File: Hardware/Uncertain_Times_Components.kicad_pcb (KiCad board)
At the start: 4 copper layers, 80.8 x 100 mm, 197 parts, among them J1 Conn_01x12_Male, J2 Conn_01x16_Male, J3 Conn_01x14_Male, J4 Conn_01x12_Male, J5 SWD_Header, J6 Eurorack_10_pin_power, J7 Audio_Breakout, J8 Gate_Breakout, Q1 MMBT3904, U1 LM1117-3.3, U10 TL074, U11 TL074, U12 TL074, U13 TL074, U14 TL074, U15 TL074, U2 STM32G473V, U3 LM1117-5.0, U4 PS508, U5 MCP6002, U6 AS3364, U7 AS3364, U8 AD5676, U9 MCP48CMB21, Y1 8MHz 20pF

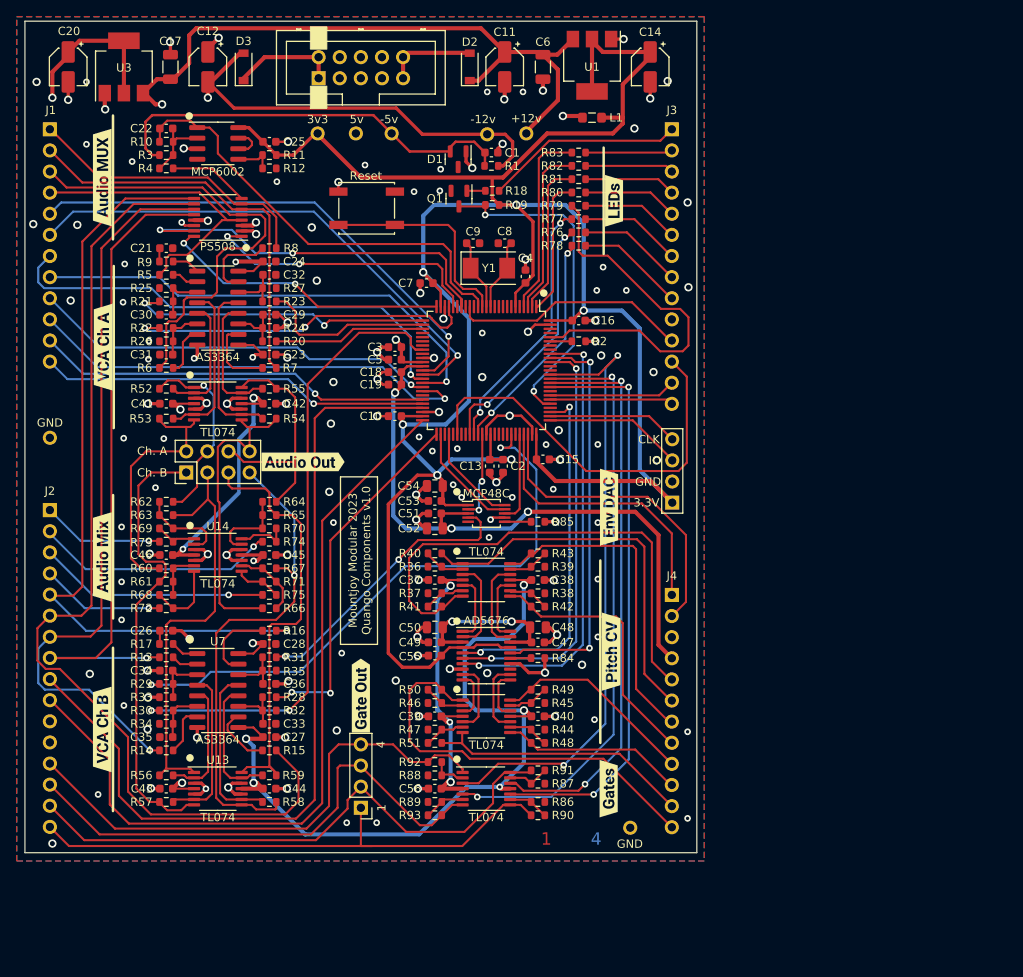
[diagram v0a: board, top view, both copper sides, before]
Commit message: Started routing components
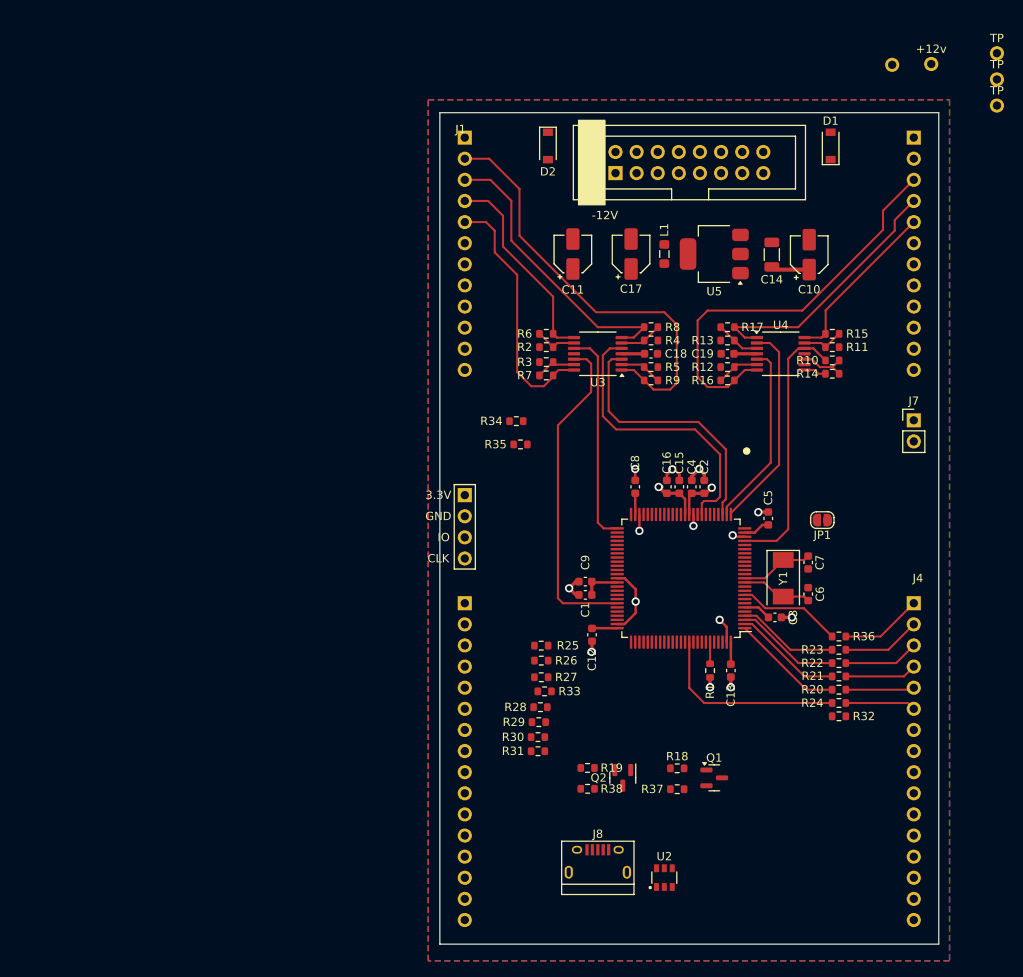
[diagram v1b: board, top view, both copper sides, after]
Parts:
- removed the C1 at (106.2, 54.8)
- removed the C17 at (67.6, 44.5)
- removed C20: 22uF, Capacitor_SMD:CP_Elec_4x5.8
- removed C21, C26: 10nF, Capacitor_SMD:C_0603_1608Metric
- removed C22: 1.5nF, Capacitor_SMD:C_0603_1608Metric
- removed C23, C24, C27, C28, C37, C38, C39, C40, C41, C42, C43, C44, C45, C46, C47, C49, C51, C53, C55, C56: 100nF, Capacitor_SMD:C_0603_1608Metric
- removed C25: 1uF, Capacitor_SMD:C_0603_1608Metric
- removed C29, C30, C31, C32, C33, C34, C35, C36: 2.2nF, Capacitor_SMD:C_0603_1608Metric
- removed C48, C50, C52, C54: 10uF, Capacitor_SMD:C_0805_2012Metric
- removed the D1 at (102.2, 55.6)
- removed FID1: Fiducial, Custom_Footprints:4_Layer_Markers
- removed the R1 at (106.2, 56.4)
- removed the R20 at (79.5, 77.5)
- removed the R21 at (67.1, 72.7)
- removed the R22 at (67.1, 75.9)
- removed the R23 at (79.5, 72.7)
- removed the R24 at (79.5, 75.9)
- removed the R25 at (67.1, 71.1)
- removed the R26 at (67.1, 77.5)
- removed the R27 at (79.5, 71.1)
- removed the R38 at (111.8, 107.8)
- removed R39, R44, R45, R46, R47, R60, R61, R62, R63, R64, R65, R66, R67, R68, R69, R70, R71, R86, R87, R88, R89: 10k, Resistor_SMD:R_0603_1608Metric
- removed R40, R41, R42, R43, R48, R49, R50, R51: 2k, Resistor_SMD:R_0603_1608Metric
- removed R52, R53, R54, R55, R56, R57, R58, R59: 30k, Resistor_SMD:R_0603_1608Metric
- removed R72, R73, R74, R75: 1k, Resistor_SMD:R_0603_1608Metric
- removed R84, R85: 560, Resistor_SMD:R_0603_1608Metric
- removed R90, R91, R92, R93: 15k, Resistor_SMD:R_0603_1608Metric
- removed RESET1: SW_Push, Custom_Footprints:SW_SPST_EVQQ2
- removed TP6, TP7: TestPoint, Custom_Footprints:1mm_Test_Point
- removed the U1 at (118.3, 44.3)
- removed U10, U11, U12, U13, U14, U15: TL074, Package_SO:TSSOP-14_4.4x5mm_P0.65mm
- removed U6, U7: AS3364, Package_SO:SOIC-16_3.9x9.9mm_P1.27mm
- removed U8: AD5676, Package_SO:TSSOP-20_4.4x6.5mm_P0.65mm
- removed U9: MCP48CMB21, Package_SO:MSOP-10_3x3mm_P0.5mm
- removed kibuzzard-646A0602: G***, kibuzzard-646A0602
- removed kibuzzard-646A061F: G***, kibuzzard-646A061F
- removed kibuzzard-646A06F2: G***, kibuzzard-646A06F2
- removed kibuzzard-646A076E: G***, kibuzzard-646A076E
- removed kibuzzard-646B918A: G***, kibuzzard-646B918A
- removed kibuzzard-646B919C: G***, kibuzzard-646B919C
- removed kibuzzard-646B91AE: G***, kibuzzard-646B91AE
- removed kibuzzard-646B91BF: G***, kibuzzard-646B91BF
- removed kibuzzard-646B935C: G***, kibuzzard-646B935C
- removed kibuzzard-646B9368: G***, kibuzzard-646B9368
- added C18: 100nF, Capacitor_SMD:C_0603_1608Metric, F.Cu at (125.4, 79.0)
- added C19: 100nF, Capacitor_SMD:C_0603_1608Metric, F.Cu at (134.6, 79.0)
- added JP1: Jumper, Jumper:SolderJumper-2_P1.3mm_Open_RoundedPad1.0x1.5mm, F.Cu at (146.0, 99.0)
- added Q1: MMBT3904, Package_TO_SOT_SMD:SOT-23, F.Cu at (133.0, 130.0)
- added R18: 4k7, Resistor_SMD:R_0603_1608Metric, F.Cu at (128.6, 128.9)
- added R2: 10k, Resistor_SMD:R_0603_1608Metric, F.Cu at (112.8, 78.2)
- added U2: STF202-22T1G, Custom_Footprints:STF202-22T1G, F.Cu at (127.0, 142.0)
- C10: renamed from C11; value 47uF -> 22uF
- J2: value Conn_01x16_Male -> Conn_01x12_Male; footprint Connector_PinHeader_2.54mm:PinHeader_1x16_P2.54mm_Vertical -> Connector_PinHeader_2.54mm:PinHeader_1x12_P2.54mm_Vertical
- J3: value Conn_01x14_Male -> Conn_01x16_Male; footprint Connector_PinHeader_2.54mm:PinHeader_1x14_P2.54mm_Vertical -> Connector_PinHeader_2.54mm:PinHeader_1x16_P2.54mm_Vertical
- J4: value Conn_01x12_Male -> Conn_01x16_Male; footprint Connector_PinHeader_2.54mm:PinHeader_1x12_P2.54mm_Vertical -> Connector_PinHeader_2.54mm:PinHeader_1x16_P2.54mm_Vertical
- J6: value Eurorack_10_pin_power -> Eurorack_16_pin_power; footprint Custom_Footprints:Eurorack_10_pin_header -> Custom_Footprints:Eurorack_16_pin_header
- J7: value Audio_Breakout -> UART_Test_Pins; footprint Connector_PinHeader_2.54mm:PinHeader_2x04_P2.54mm_Vertical -> Connector_PinHeader_2.54mm:PinHeader_1x02_P2.54mm_Vertical
- J8: value Gate_Breakout -> USB_B_Micro; footprint Connector_PinHeader_2.54mm:PinHeader_1x04_P2.54mm_Vertical -> Custom_Footprints:USB_Micro-B_Amphenol
- R10: value 6k8 -> 10k
- R13, R15, R16, R5, R6, R7, R8: value 30k -> 10k
- R14: value 30k -> 20k
- R17, R9: value 100R -> 10k
- R28, R29, R30, R31: value 6k8 -> 560
- R3: value 20k -> 10k
- R32, R33, R34, R35, R36: value 10k -> 560
- R37: value 10k -> 4k7
- R4: value 47k -> 10k
- U3: value LM1117-5.0 -> TL074; footprint Package_TO_SOT_SMD:SOT-223-3_TabPin2 -> Package_SO:TSSOP-14_4.4x5mm_P0.65mm
- U4: value PS508 -> TL074; footprint Package_SO:TSSOP-16_4.4x5mm_P0.65mm -> Package_SO:TSSOP-14_4.4x5mm_P0.65mm
- U5: value MCP6002 -> LT1117-3.3; footprint Package_SO:SOIC-8_3.9x4.9mm_P1.27mm -> Package_TO_SOT_SMD:SOT-223-3_TabPin2
- moved J2 113.1 mm to (157.0, 53.0)
- moved R14 92.0 mm to (147.2, 81.4), turned to 0 degrees
- moved J7 87.7 mm to (157.0, 87.0), turned to 0 degrees
- moved R10 84.3 mm to (147.2, 79.8), turned to 180 degrees
- moved R15 84.2 mm to (147.2, 76.6)
- moved TP5 81.8 mm to (167.0, 49.1)
- moved TP3 77.7 mm to (167.0, 42.9)
- moved R13 77.5 mm to (134.6, 77.4), turned to 0 degrees
- moved R17 77.5 mm to (134.6, 75.8), turned to 180 degrees
- moved TP4 73.1 mm to (167.0, 46.0)
- moved Q2 72.4 mm to (122.0, 130.0)
- moved R11 71.5 mm to (147.2, 78.2), turned to 180 degrees
- moved R38 71.2 mm to (117.8, 131.3)
- moved R19 70.4 mm to (117.8, 128.8)
- moved U4 69.7 mm to (141.0, 79.0), turned to 0 degrees
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- renumbered C2 to C1, C12 to C11, C15 to C12, C16 to C13, C6 to C14, C18 to C15, C19 to C16, C14 to C17, C3 to C2, C4 to C3, C5 to C4, C7 to C5, C8 to C6, C9 to C7, C10 to C8, C13 to C9, D2 to D1, D3 to D2, Q1 to Q2, R2 to R1, R18 to R19, R76 to R20, R77 to R21, R78 to R22, R79 to R23, R80 to R24, R81 to R25, R82 to R26, R83 to R27, R19 to R38, U2 to U1
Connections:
- J1 pad 1: /AudioA4_In -> GND
- J1 pad 10: /Env2_Decay -> GND
- J1 pad 11: /Env2_Sustain -> /Sine1_Level
- J1 pad 12: /Env2_Release -> /Sine2_Level
- J1 pad 2: /AudioA3_In -> /FM3_Out
- J1 pad 3: /AudioA2_In -> /FM2_Out
- J1 pad 4: /AudioA1_In -> /Ramp_Out
- J1 pad 5: /Env1_Attack -> /Swell_Out
- J1 pad 6: /Env1_Decay -> /Sine2_Rate_Btn
- J1 pad 7: /Env1_Sustain -> /Sine3_Rate_Btn
- J1 pad 8: /Env1_Release -> /Sine1_Swell_Rate_LED
- J1 pad 9: /Env2_Attack -> unconnected-(J1-Pin_9-Pad9)
- J2 pad 1: /Audio2_Out -> GND
- J2 pad 10: /Calib_Btn2 -> GND
- J2 pad 11: +3.3VA -> /Sine3_Level
- J2 pad 12: GND -> /Sine1_Rate
- J2 pad 2: /Audio3_Out -> +3.3V
- J2 pad 3: /Audio4_Out -> /Sine2_Out
- J2 pad 4: /Audio1_Out -> /Sine3_Out
- J2 pad 5: /AudioB4_In -> /Sine1_Out
- J2 pad 6: /AudioB3_In -> /Sine2_Lvl_Btn
- J2 pad 7: /AudioB2_In -> /Sine1_Rate_Btn
- J2 pad 8: /AudioB1_In -> /Sine1_Inv_Out
- J2 pad 9: /Calib_Btn1 -> +3.3VA
- J3 pad 1: /MIDI_IN -> GND
- J3 pad 10: GND -> /Sine3_Swell_Lvl_LED
- J3 pad 11: /ChannelA_Level -> /Sine1_Ramp_Rate_LED
- J3 pad 12: /ChannelB_Level -> /Sine3_Lvl_Btn
- J3 pad 13: /Test_Pin1 -> /Sine3_Rate
- J3 pad 14: /Test_Pin2 -> /Clock_In
- J3 pad 2: /EnvA4_LED_Out -> /Sine3_Ramp_Rate_LED
- J3 pad 3: /EnvA3_LED_Out -> /Sine1_Ramp_Lvl_LED
- J3 pad 4: /EnvA2_LED_Out -> /Sine2_Ramp_Lvl_LED
- J3 pad 5: /EnvA1_LED_Out -> /Sine3_Ramp_Lvl_LED
- J3 pad 6: /EnvB4_LED_Out -> /Sine1_Swell_Lvl_LED
- J3 pad 7: /EnvB2_LED_Out -> /Sine2_Swell_Rate_LED
- J3 pad 8: /EnvB1_LED_Out -> /Sine2_Swell_Lvl_LED
- J3 pad 9: /EnvB3_LED_Out -> unconnected-(J3-Pin_9-Pad9)
- J4 pad 1: /USB_DM -> /Sine3_Swell_Rate_LED
- J4 pad 10: /CV_OUT_B1 -> unconnected-(J4-Pin_10-Pad10)
- J4 pad 11: /CV_OUT_B4 -> /Sine2_Ramp_Rate_LED
- J4 pad 12: /CV_OUT_B3 -> unconnected-(J4-Pin_12-Pad12)
- J4 pad 2: /USB_DP -> /Sine2_LED
- J4 pad 3: GND -> /Sine1_LED
- J4 pad 4: +3.3VA -> /Swell_LED
- J4 pad 5: /CV_OUT_A2 -> /Ramp_LED
- J4 pad 6: /CV_OUT_A1 -> /Sine3_LED
- J4 pad 7: /CV_OUT_A4 -> unconnected-(J4-Pin_7-Pad7)
- J4 pad 8: /CV_OUT_A3 -> unconnected-(J4-Pin_8-Pad8)
- J4 pad 9: /CV_OUT_B2 -> GND
- J7 pad 1: /OpAmps/AudioB1_Out -> /USART1_TX
- J7 pad 2: /OpAmps/AudioA1_Out -> /USART1_RX
- J8 pad 1: /Gate1_Out -> unconnected-(J8-VBUS-Pad1)
- J8 pad 2: /Gate2_Out -> /USB_D-
- J8 pad 3: /Gate3_Out -> /USB_D+
- J8 pad 4: /Gate4_Out -> unconnected-(J8-ID-Pad4)
- Q2 pad 3: /MIDI_UART -> /Clock_Scaled
- R10 pad 1: /Audio_In_Multiplexed -> Net-(U4C-+)
- R10 pad 2: Net-(C22-Pad2) -> /Sine1_DAC
- R11 pad 1: Net-(R11-Pad1) -> GND
- R11 pad 2: +3.3V -> Net-(U4D--)
- R12 pad 2: Net-(R11-Pad1) -> Net-(U4B--)
- R13 pad 1: Net-(R13-Pad1) -> GND
- R13 pad 2: /AudioB1_In -> Net-(U4A-+)
- R14 pad 1: Net-(R14-Pad1) -> /Sine1_Inv_Out
- R14 pad 2: /AudioB2_In -> Net-(U4C-+)
- R15 pad 1: Net-(R15-Pad1) -> /Sine1_Out
- R15 pad 2: /AudioB3_In -> Net-(U4D--)
- R16 pad 1: Net-(R16-Pad1) -> /Sine2_Out
- R16 pad 2: /AudioB4_In -> Net-(U4B--)
- R17 pad 1: Net-(C26-Pad1) -> /Sine3_Out
- R17 pad 2: Net-(R17-Pad2) -> Net-(U4A-+)
- R19 pad 1: /MIDI_IN -> /Clock_In
- R20 pad 1: /EnvB1_LED_Out -> /Ramp_LED
- R20 pad 2: /EnvB1_LED -> /TIM3_CH1
- R21 pad 1: /EnvB2_LED_Out -> /Swell_LED
- R21 pad 2: /EnvB2_LED -> /TIM3_CH2
- R22 pad 1: /EnvB3_LED_Out -> /Sine1_LED
- R22 pad 2: /EnvB3_LED -> /TIM3_CH3
- R23 pad 1: /EnvB4_LED_Out -> /Sine2_LED
- R23 pad 2: /EnvB4_LED -> /TIM3_CH4
- R24 pad 1: /EnvA1_LED_Out -> /Sine3_LED
- R24 pad 2: /EnvA1_LED -> /TIM2_CH2
- R25 pad 1: /EnvA2_LED_Out -> /Sine1_Ramp_Lvl_LED
- R25 pad 2: /EnvA2_LED -> /TIM4_CH2
- R26 pad 1: /EnvA3_LED_Out -> /Sine2_Ramp_Lvl_LED
- R26 pad 2: /EnvA3_LED -> /TIM4_CH3
- R27 pad 1: /EnvA4_LED_Out -> /Sine3_Ramp_Lvl_LED
- R27 pad 2: /EnvA4_LED -> /TIM4_CH4
- R28 pad 1: /EnvB3_DAC -> /Sine1_Swell_Lvl_LED
- R28 pad 2: /EnvB3_Scaled -> /TIM8_CH1
- R29 pad 1: /EnvB1_DAC -> /Sine2_Swell_Lvl_LED
- R29 pad 2: /EnvB1_Scaled -> /TIM8_CH2
- R3 pad 1: Net-(C22-Pad2) -> GND
- R3 pad 2: /-5V_REF -> Net-(U3D--)
- R30 pad 1: /EnvB2_DAC -> /Sine3_Swell_Lvl_LED
- R30 pad 2: /EnvB2_Scaled -> /TIM8_CH3
- R31 pad 1: /EnvB4_DAC -> /Sine1_Ramp_Rate_LED
- R31 pad 2: /EnvB4_Scaled -> /TIM8_CH4
- R32 pad 1: /EnvB3_Scaled -> /Sine2_Ramp_Rate_LED
- R32 pad 2: GND -> /TIM2_CH1
- R33 pad 1: /EnvB1_Scaled -> /Sine3_Ramp_Rate_LED
- R33 pad 2: GND -> /TIM4_CH1
- R34 pad 1: /EnvB2_Scaled -> /Sine1_Swell_Rate_LED
- R34 pad 2: GND -> /TIM2_CH3
- R35 pad 1: /EnvB4_Scaled -> /Sine2_Swell_Rate_LED
- R35 pad 2: GND -> /TIM2_CH4
- R36 pad 1: GND -> /Sine3_Swell_Rate_LED
- R36 pad 2: Net-(R36-Pad2) -> /Sine3_Swell_Rate
- R37 pad 1: GND -> /Gate_Scaled
- R37 pad 2: Net-(R37-Pad2) -> +3.3V
- R38 pad 1: /MIDI_UART -> /Clock_Scaled
- R4 pad 1: Net-(C22-Pad2) -> GND
- R4 pad 2: Net-(R4-Pad2) -> Net-(U3B--)
- R5 pad 1: Net-(R5-Pad1) -> GND
- R5 pad 2: /AudioA1_In -> Net-(U3A--)
- R6 pad 1: Net-(R6-Pad1) -> /Ramp_Out
- R6 pad 2: /AudioA2_In -> Net-(U3C--)
- R7 pad 1: Net-(R7-Pad1) -> /Swell_Out
- R7 pad 2: /AudioA3_In -> Net-(U3D--)
- R8 pad 1: Net-(R8-Pad1) -> /FM2_Out
- R8 pad 2: /AudioA4_In -> Net-(U3B--)
- R9 pad 1: Net-(C21-Pad1) -> /FM3_Out
- R9 pad 2: Net-(R9-Pad2) -> Net-(U3A--)
- TP3 pad 1: +5V -> +3.3V
- TP4 pad 1: /-5V_REF -> GND
- TP5 pad 1: +3.3V -> GND
- U1 pad 1: /EnvA1_LED -> /TIM3_CH1
- U1 pad 15: /Audio_In_Multiplexed -> /ADC-Spare
- U1 pad 17: /ChannelA_Level -> /Swell_Level
- U1 pad 19: /MultiplexerA2 -> unconnected-(U1-PF2-Pad19)
- U1 pad 2: /EnvA2_LED -> /TIM3_CH2
- U1 pad 21: /MultiplexerA0 -> unconnected-(U1-PA1-Pad21)
- U1 pad 22: /EnvA2_DAC -> /Sine1_DAC
- U1 pad 25: /MultiplexerA1 -> unconnected-(U1-PA3-Pad25)
- U1 pad 26: /EnvA1_DAC -> /Sine3_DAC
- U1 pad 27: /EnvA4_DAC -> /Sine2_DAC
- U1 pad 28: /EnvA3_DAC -> /FM3_DAC
- U1 pad 3: /EnvA3_LED -> /TIM3_CH3
- U1 pad 30: unconnected-(U2-Pad30) -> /USART1_TX
- U1 pad 31: unconnected-(U2-Pad31) -> /USART1_RX
- U1 pad 33: /EnvB2_DAC -> /FM2_DAC
- U1 pad 38: /Env1_Attack -> /Sine3_Level
- U1 pad 39: /Env1_Decay -> /Sine1_Rate
- U1 pad 4: /EnvA4_LED -> /TIM3_CH4
- U1 pad 40: /Env1_Sustain -> /Sine1_Level
- U1 pad 41: /Env1_Release -> /Sine2_Level
- U1 pad 42: /Env2_Attack -> /Sine2_Rate
- U1 pad 43: /Env2_Decay -> /Sine3_Rate
- U1 pad 45: /Env2_Sustain -> /Ramp_Rate
- U1 pad 46: /Env2_Release -> /Ramp_Level
- U1 pad 47: /Calib_Btn1 -> /TIM2_CH3
- U1 pad 50: /Calib_Btn2 -> /TIM2_CH4
- U1 pad 51: /EnvB3_DAC -> /Ramp_DAC
- U1 pad 52: /SPI2_SCK -> unconnected-(U1-PB13-Pad52)
- U1 pad 54: /SPI2_MOSI -> unconnected-(U1-PB15-Pad54)
- U1 pad 56: /ChannelB_Level -> /Swell_Rate
- U1 pad 59: /EnvB1_LED -> /TIM4_CH1
- U1 pad 60: /EnvB2_LED -> /TIM4_CH2
- U1 pad 61: /EnvB3_LED -> /TIM4_CH3
- U1 pad 62: /SPI2_NSS -> /TIM4_CH4
- U1 pad 65: unconnected-(U2-Pad65) -> /TIM8_CH1
- U1 pad 66: unconnected-(U2-Pad66) -> /TIM8_CH2
- U1 pad 67: unconnected-(U2-Pad67) -> /TIM8_CH3
- U1 pad 68: unconnected-(U2-Pad68) -> /TIM8_CH4
- U1 pad 69: /EnvB1_DAC -> /Swell_DAC
- U1 pad 71: /SPI2_MISO -> unconnected-(U1-PA10-Pad71)
- U1 pad 78: /SPI1_NSS -> /TIM2_CH1
- U1 pad 80: /MIDI_UART -> unconnected-(U1-PC11-Pad80)
- U1 pad 81: /Test_Pin2 -> /Clock_Scaled
- U1 pad 82: /Test_Pin1 -> /Sine1_Lvl_Btn
- U1 pad 83: unconnected-(U2-Pad83) -> /Sine2_Lvl_Btn
- U1 pad 84: /Gate1 -> /Sine3_Lvl_Btn
- U1 pad 85: /Gate2 -> /Sine1_Rate_Btn
- U1 pad 86: /Gate3 -> /Sine2_Rate_Btn
- U1 pad 87: /Gate4 -> /Sine3_Rate_Btn
- U1 pad 89: unconnected-(U2-Pad89) -> /Gate_Scaled
- U1 pad 9: unconnected-(U2-Pad9) -> /Sine3_Swell_Rate
- U1 pad 90: /SPI1_SCK -> /TIM2_CH2
- U1 pad 91: /SPI1_MISO -> unconnected-(U1-PB4-Pad91)
- U1 pad 92: /SPI1_MOSI -> unconnected-(U1-PB5-Pad92)
- U1 pad 96: /EnvB4_LED -> unconnected-(U1-PB9-Pad96)
- U3 pad 1: GND -> /FM3_Out
- U3 pad 2: +5V -> Net-(U3A--)
- U3 pad 3: +12V -> /FM3_DAC
- U4 pad 1: /MultiplexerA0 -> /Sine3_Out
- U4 pad 10: /AudioB3_In -> Net-(U4C-+)
- U4 pad 11: /AudioB2_In -> -12V
- U4 pad 12: /AudioB1_In -> /Sine1_DAC
- U4 pad 13: +12V -> Net-(U4D--)
- U4 pad 14: GND -> /Sine1_Out
- U4 pad 2: +3.3V -> /Sine3_DAC
- U4 pad 3: -12V -> Net-(U4A-+)
- U4 pad 4: /AudioA1_In -> +12V
- U4 pad 5: /AudioA2_In -> /Sine2_DAC
- U4 pad 6: /AudioA3_In -> Net-(U4B--)
- U4 pad 7: /AudioA4_In -> /Sine2_Out
- U4 pad 8: Net-(R4-Pad2) -> /Sine1_Inv_Out
- U4 pad 9: /AudioB4_In -> GND
- U5 pad 1: /Audio_In_Multiplexed -> GND
- U5 pad 2: Net-(C22-Pad2) -> +3.3V
- U5 pad 3: GND -> +12V
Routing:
- net +3.3V: track 319.0 -> 19.5 mm, vias 7 -> 0
- net -12V: track 266.4 -> 0.00 mm, vias 10 -> 0
- net +12V: track 264.8 -> 9.30 mm, vias 10 -> 0
- net +3.3VA: track 229.7 -> 17.4 mm, vias 5 -> 2
- net +5V: track 146.3 -> 0.00 mm, vias 3 -> 0
- net /AudioB3_In: track 120.0 -> 0.00 mm
- net GND: track 138.7 -> 33.7 mm, vias 134 -> 14
- net /Calib_Btn1: track 102.5 -> 0.00 mm
- net /Calib_Btn2: track 94.1 -> 0.00 mm
- net /AudioB4_In: track 93.1 -> 0.00 mm, vias 1 -> 0
- net /AudioB2_In: track 89.3 -> 0.00 mm, vias 1 -> 0
- net /AudioB1_In: track 80.3 -> 0.00 mm, vias 1 -> 0
- net /EnvB2_DAC: track 75.5 -> 0.00 mm, vias 2 -> 0
- net /Gate4: track 74.3 -> 0.00 mm, vias 2 -> 0
- net /Gate3: track 72.0 -> 0.00 mm, vias 2 -> 0
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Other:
- board size 80.8 x 100 mm -> 60 x 100 mm
- board text removed: "1"
- board text removed: "4"
- board text removed: "Ch. A"
- board text removed: "Ch. B"
- board text removed: "J2"
- board text removed: "J3"
- board text removed: "MCP48C"
- board text removed: "Mountjoy Modular 2023 Quango Components v1.0"
- board text removed: "Reset"

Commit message: Signal Routing done
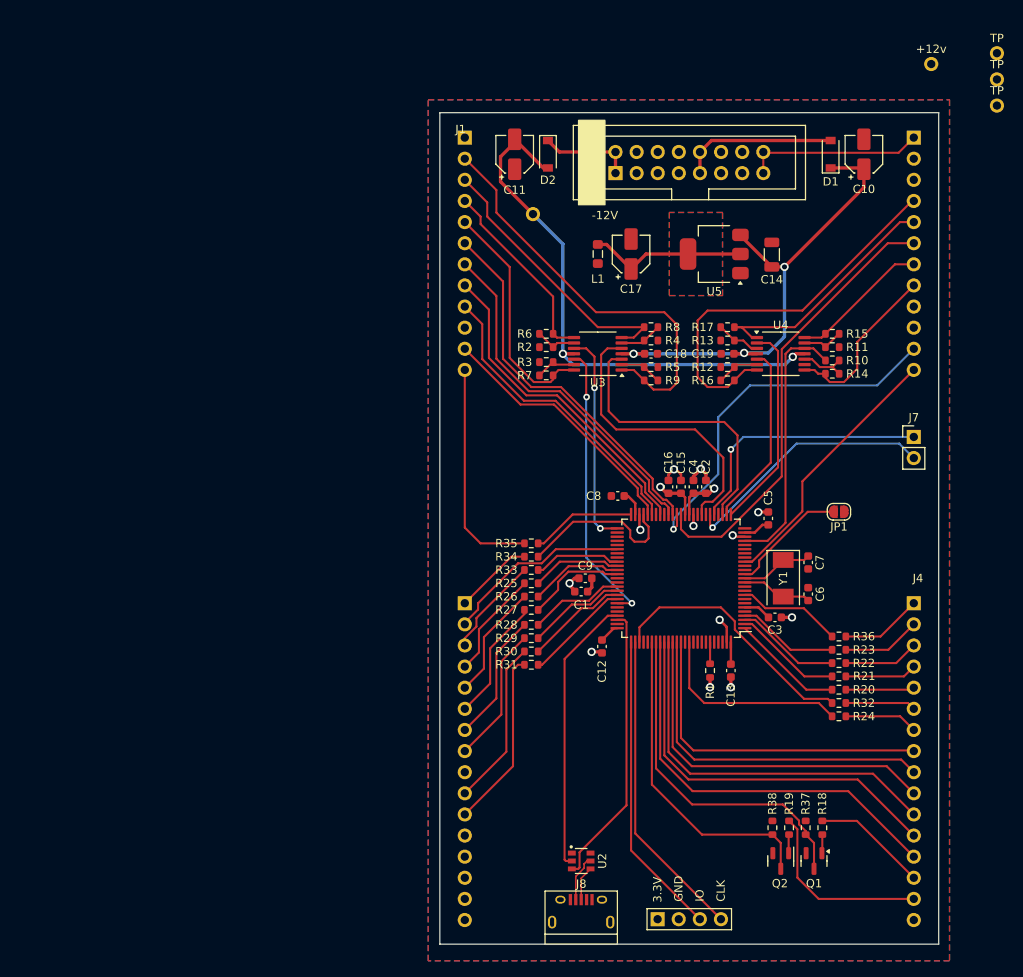
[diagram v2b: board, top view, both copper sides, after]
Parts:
- moved J5 56.0 mm to (126.2, 147.0), turned to 0 degrees
- moved TP2 46.8 mm to (111.2, 62.2)
- moved R19 25.3 mm to (142.0, 136.0), turned to -90 degrees
- moved R38 22.7 mm to (140.0, 136.0), turned to 90 degrees
- moved Q2 21.5 mm to (141.0, 140.0)
- moved R18 18.9 mm to (146.0, 136.0), turned to -90 degrees
- moved R34 16.4 mm to (111.0, 103.4)
- moved R37 16.1 mm to (144.0, 136.0), turned to 90 degrees
- moved Q1 15.6 mm to (145.0, 140.0), turned to -90 degrees
- moved R33 14.7 mm to (111.0, 105.0), turned to 0 degrees
- moved C11 13.9 mm to (109.0, 55.0)
- moved C10 13.7 mm to (151.0, 55.0)
- moved R35 12.0 mm to (111.0, 101.8)
- moved R31 10.4 mm to (111.0, 116.4)
- moved R30 10.3 mm to (111.0, 114.8)
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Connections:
- J1 pad 10: GND -> unconnected-(J1-Pin_10-Pad10)
- J1 pad 11: /Sine1_Level -> /Ramp_Level
- J1 pad 12: /Sine2_Level -> /Sine2_Swell_Rate_LED
- J1 pad 6: /Sine2_Rate_Btn -> /Sine1_Level
- J1 pad 7: /Sine3_Rate_Btn -> /Sine2_Level
- J1 pad 8: /Sine1_Swell_Rate_LED -> /Sine3_Rate
- J1 pad 9: unconnected-(J1-Pin_9-Pad9) -> /Ramp_Rate
- J2 pad 1: GND -> /Gate_Normal
- J2 pad 11: /Sine3_Level -> /Sine1_Rate
- J2 pad 12: /Sine1_Rate -> /Swell_Level
- J2 pad 2: +3.3V -> GND
- J2 pad 3: /Sine2_Out -> +3.3V
- J2 pad 4: /Sine3_Out -> /Sine2_Out
- J2 pad 5: /Sine1_Out -> /Sine3_Out
- J2 pad 6: /Sine2_Lvl_Btn -> /Sine3_Level
- J2 pad 7: /Sine1_Rate_Btn -> /Sine1_Out
- J3 pad 1: GND -> /Sine1_Swell_Rate_LED
- J3 pad 12: /Sine3_Lvl_Btn -> unconnected-(J3-Pin_12-Pad12)
- J3 pad 13: /Sine3_Rate -> unconnected-(J3-Pin_13-Pad13)
- J3 pad 14: /Clock_In -> unconnected-(J3-Pin_14-Pad14)
- J3 pad 15: /Ramp_Rate -> unconnected-(J3-Pin_15-Pad15)
- J3 pad 16: /Ramp_Level -> unconnected-(J3-Pin_16-Pad16)
- J3 pad 2: /Sine3_Ramp_Rate_LED -> /Swell_Rate
- J3 pad 3: /Sine1_Ramp_Lvl_LED -> /Sine3_Ramp_Rate_LED
- J3 pad 4: /Sine2_Ramp_Lvl_LED -> /Sine1_Ramp_Lvl_LED
- J3 pad 5: /Sine3_Ramp_Lvl_LED -> /Sine2_Ramp_Lvl_LED
- J3 pad 6: /Sine1_Swell_Lvl_LED -> /Sine3_Ramp_Lvl_LED
- J3 pad 7: /Sine2_Swell_Rate_LED -> /Sine1_Swell_Lvl_LED
- J4 pad 10: unconnected-(J4-Pin_10-Pad10) -> /Sine1_Rate_Btn
- J4 pad 11: /Sine2_Ramp_Rate_LED -> /Sine3_Lvl_Btn
- J4 pad 12: unconnected-(J4-Pin_12-Pad12) -> /Sine2_Lvl_Btn
- J4 pad 13: /Swell_Rate -> /Sine1_Lvl_Btn
- J4 pad 14: /Swell_Level -> /Gate_In
- J4 pad 15: GND -> /Clock_In
- J4 pad 16: /Gate_In -> GND
- J4 pad 6: /Sine3_LED -> /Sine2_Ramp_Rate_LED
- J4 pad 7: unconnected-(J4-Pin_7-Pad7) -> /Sine3_LED
- J4 pad 8: unconnected-(J4-Pin_8-Pad8) -> /Sine3_Rate_Btn
- J4 pad 9: GND -> /Sine2_Rate_Btn
- U1 pad 82: /Sine1_Lvl_Btn -> /Gate_Scaled
- U1 pad 83: /Sine2_Lvl_Btn -> /Sine1_Lvl_Btn
- U1 pad 84: /Sine3_Lvl_Btn -> /Sine2_Lvl_Btn
- U1 pad 85: /Sine1_Rate_Btn -> /Sine3_Lvl_Btn
- U1 pad 86: /Sine2_Rate_Btn -> /Sine1_Rate_Btn
- U1 pad 87: /Sine3_Rate_Btn -> /Sine2_Rate_Btn
- U1 pad 88: unconnected-(U1-PD6-Pad88) -> /Sine3_Rate_Btn
- U1 pad 89: /Gate_Scaled -> unconnected-(U1-PD7-Pad89)
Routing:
- net -12V: track 0.00 -> 66.6 mm, vias 0 -> 2
- net /Sine3_Level: track 0.00 -> 53.7 mm
- net +12V: track 9.30 -> 59.6 mm, vias 0 -> 3
- net /Sine1_Lvl_Btn: track 0.00 -> 49.4 mm
- net /Sine2_Lvl_Btn: track 0.00 -> 47.6 mm
- net /Sine3_Lvl_Btn: track 0.00 -> 45.8 mm
- net /Sine1_Level: track 0.00 -> 45.3 mm
- net /Sine1_Rate: track 0.00 -> 44.6 mm, vias 0 -> 1
- net /Sine1_Rate_Btn: track 0.00 -> 43.9 mm
- net /Sine2_Level: track 0.00 -> 42.6 mm
- net /Sine2_Rate_Btn: track 0.00 -> 42.0 mm
- net /Gate_Scaled: track 0.00 -> 41.5 mm
- net /Sine3_Rate_Btn: track 0.00 -> 40.2 mm
- net /Sine3_Rate: track 0.00 -> 39.4 mm
- net /Clock_Scaled: track 0.00 -> 38.6 mm
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- added copper zone on B.Cu, net +3.3V
- added copper zone on F.Cu, net +3.3V
- added copper zone on In1.Cu, net +3.3V
- added copper zone on In2.Cu, net +3.3V
